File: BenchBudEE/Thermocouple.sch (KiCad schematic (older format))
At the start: 22 parts, among them P2 CONN_3X2, P3 CONN_2, U2 MCP3901, U3 LMT84, U4 OPA4170

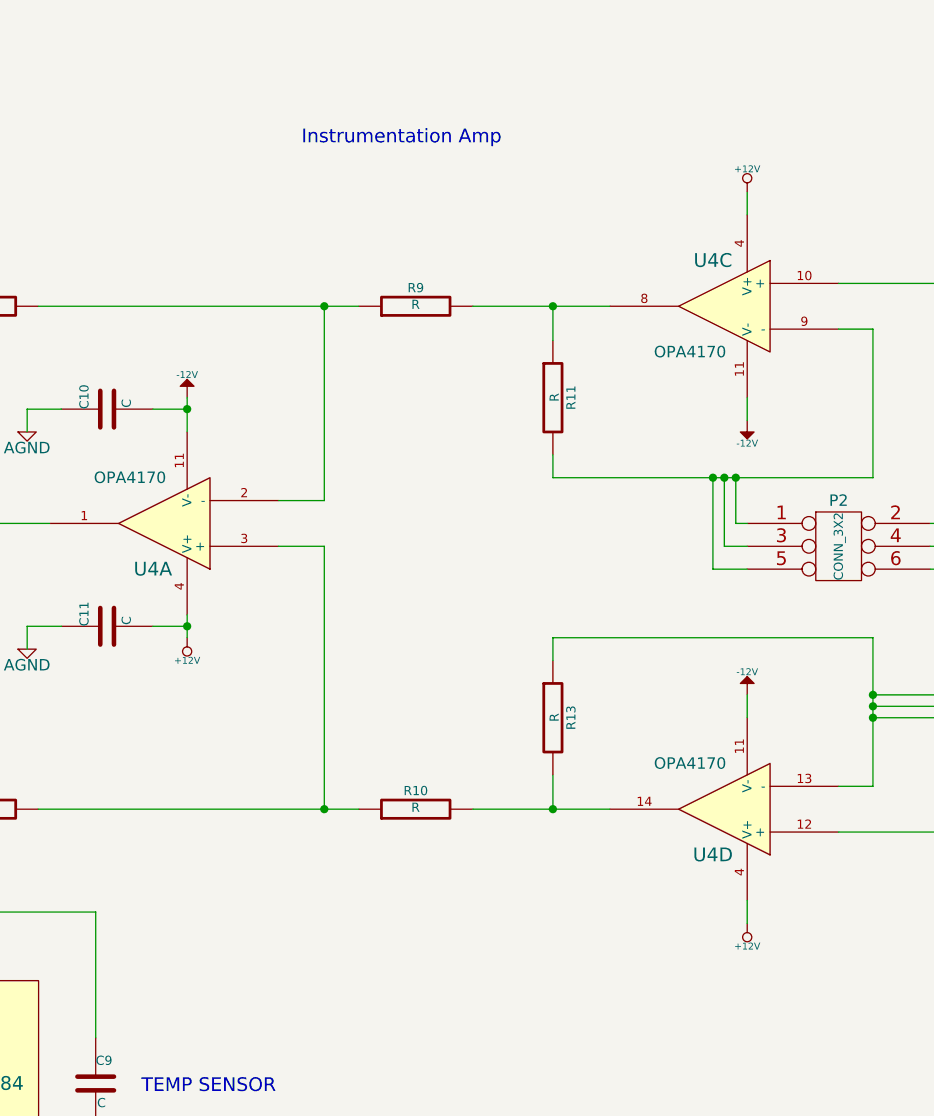
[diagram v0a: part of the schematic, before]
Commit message: Ground and Power Planes
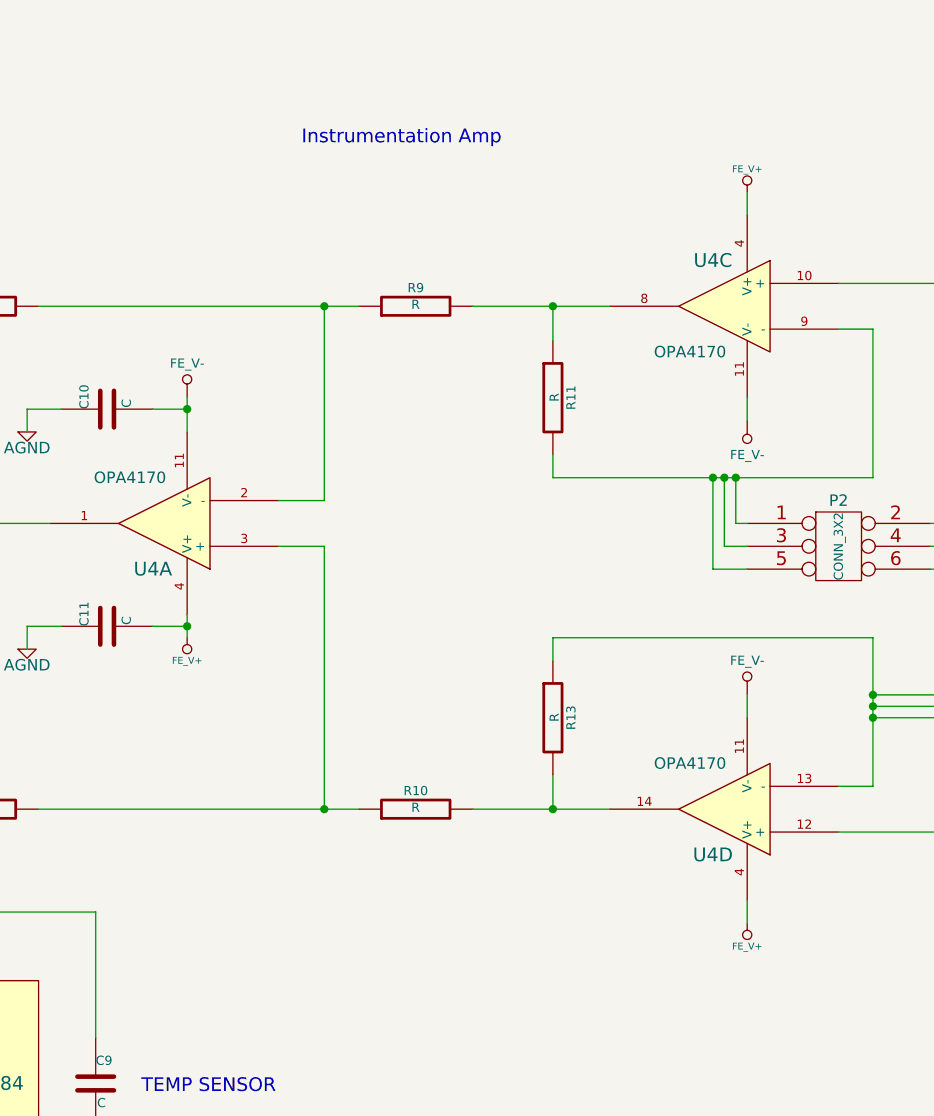
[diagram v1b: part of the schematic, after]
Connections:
- net +12V renamed FE_V+
- net -12V renamed FE_V-
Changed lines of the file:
@@
 Sheet 2 9
 Title ""
-Date "27 feb 2014"
+Date "1 mar 2014"
 Rev ""
 Comp ""
@@
 $EndComp
 $Comp
-L -12V #PWR01
-U 1 1 52F12CF6
-P 6750 2600
-F 0 "#PWR01" H 6750 2730 20  0001 C CNN
-F 1 "-12V" H 6750 2700 30  0000 C CNN
-F 2 "" H 6750 2600 60  0000 C CNN
-F 3 "" H 6750 2600 60  0000 C CNN
-	1    6750 2600
-	1    0    0    -1
-$EndComp
-$Comp
-L -12V #PWR02
-U 1 1 52F12D03
-P 9200 2700
-F 0 "#PWR02" H 9200 2830 20  0001 C CNN
-F 1 "-12V" H 9200 2800 30  0000 C CNN
-F 2 "" H 9200 2700 60  0000 C CNN
-F 3 "" H 9200 2700 60  0000 C CNN
-	1    9200 2700
-	-1   0    0    1
-$EndComp
-$Comp
-L -12V #PWR03
-U 1 1 52F12D09
-P 9200 3900
-F 0 "#PWR03" H 9200 4030 20  0001 C CNN
-F 1 "-12V" H 9200 4000 30  0000 C CNN
-F 2 "" H 9200 3900 60  0000 C CNN
-F 3 "" H 9200 3900 60  0000 C CNN
-	1    9200 3900
-	1    0    0    -1
-$EndComp
-$Comp
-L +12V #PWR04
-U 1 1 52F12D6E
-P 6750 3650
-F 0 "#PWR04" H 6750 3600 20  0001 C CNN
-F 1 "+12V" H 6750 3750 30  0000 C CNN
-F 2 "" H 6750 3650 60  0000 C CNN
-F 3 "" H 6750 3650 60  0000 C CNN
-	1    6750 3650
-	-1   0    0    1
-$EndComp
-$Comp
-L +12V #PWR05
-U 1 1 52F12D7B
-P 9200 1700
-F 0 "#PWR05" H 9200 1650 20  0001 C CNN
-F 1 "+12V" H 9200 1800 30  0000 C CNN
-F 2 "" H 9200 1700 60  0000 C CNN
-F 3 "" H 9200 1700 60  0000 C CNN
-	1    9200 1700
-	1    0    0    -1
-$EndComp
-$Comp
-L +12V #PWR06
-U 1 1 52F12D81
-P 9200 4900
-F 0 "#PWR06" H 9200 4850 20  0001 C CNN
-F 1 "+12V" H 9200 5000 30  0000 C CNN
-F 2 "" H 9200 4900 60  0000 C CNN
-F 3 "" H 9200 4900 60  0000 C CNN
-	1    9200 4900
-	-1   0    0    1
-$EndComp
-$Comp
-L AGND #PWR07
+L AGND #PWR7
 U 1 1 52F12E22
 P 5250 4550
-F 0 "#PWR07" H 5250 4550 40  0001 C CNN
+F 0 "#PWR7" H 5250 4550 40  0001 C CNN
 F 1 "AGND" H 5250 4480 50  0000 C CNN
 F 2 "" H 5250 4550 60  0000 C CNN
@@
 $EndComp
 $Comp
-L AGND #PWR08
+L AGND #PWR8
 U 1 1 52F1304C
 P 5250 6650
-F 0 "#PWR08" H 5250 6650 40  0001 C CNN
+F 0 "#PWR8" H 5250 6650 40  0001 C CNN
 F 1 "AGND" H 5250 6580 50  0000 C CNN
 F 2 "" H 5250 6650 60  0000 C CNN
@@
 $EndComp
 $Comp
-L +5V #PWR09
+L +5V #PWR9
 U 1 1 5303ACCB
 P 5800 4800
-F 0 "#PWR09" H 5800 4890 20  0001 C CNN
+F 0 "#PWR9" H 5800 4890 20  0001 C CNN
 F 1 "+5V" H 5800 4890 30  0000 C CNN
 F 2 "" H 5800 4800 60  0000 C CNN
@@
 $EndComp
 $Comp
-L AGND #PWR010
+L AGND #PWR11
 U 1 1 5303AEFA
 P 6050 3700
-F 0 "#PWR010" H 6050 3700 40  0001 C CNN
+F 0 "#PWR11" H 6050 3700 40  0001 C CNN
 F 1 "AGND" H 6050 3630 50  0000 C CNN
 F 2 "" H 6050 3700 60  0000 C CNN
@@
 $EndComp
 $Comp
-L AGND #PWR011
+L AGND #PWR10
 U 1 1 5303AFBF
 P 6050 2750
-F 0 "#PWR011" H 6050 2750 40  0001 C CNN
+F 0 "#PWR10" H 6050 2750 40  0001 C CNN
 F 1 "AGND" H 6050 2680 50  0000 C CNN
 F 2 "" H 6050 2750 60  0000 C CNN
@@
 $EndComp
 $Comp
-L +5V #PWR012
+L +5V #PWR4
 U 1 1 5303B53D
 P 3200 1550
-F 0 "#PWR012" H 3200 1640 20  0001 C CNN
+F 0 "#PWR4" H 3200 1640 20  0001 C CNN
 F 1 "+5V" H 3200 1640 30  0000 C CNN
 F 2 "" H 3200 1550 60  0000 C CNN
@@
 $EndComp
 $Comp
-L AGND #PWR013
+L AGND #PWR6
 U 1 1 5303B6E8
 P 3850 1800
-F 0 "#PWR013" H 3850 1800 40  0001 C CNN
+F 0 "#PWR6" H 3850 1800 40  0001 C CNN
 F 1 "AGND" H 3850 1730 50  0000 C CNN
 F 2 "" H 3850 1800 60  0000 C CNN
@@
 $EndComp
 $Comp
-L AGND #PWR014
+L AGND #PWR3
 U 1 1 5303B92C
 P 2650 4550
-F 0 "#PWR014" H 2650 4550 40  0001 C CNN
+F 0 "#PWR3" H 2650 4550 40  0001 C CNN
 F 1 "AGND" H 2650 4480 50  0000 C CNN
 F 2 "" H 2650 4550 60  0000 C CNN
@@
 $EndComp
 $Comp
-L AGND #PWR015
+L AGND #PWR5
 U 1 1 5303BA18
 P 3200 4550
-F 0 "#PWR015" H 3200 4550 40  0001 C CNN
+F 0 "#PWR5" H 3200 4550 40  0001 C CNN
 F 1 "AGND" H 3200 4480 50  0000 C CNN
 F 2 "" H 3200 4550 60  0000 C CNN
@@
 $EndComp
 $Comp
-L +5V #PWR016
+L +5V #PWR2
 U 1 1 5303BA92
 P 2650 1550
-F 0 "#PWR016" H 2650 1640 20  0001 C CNN
+F 0 "#PWR2" H 2650 1640 20  0001 C CNN
 F 1 "+5V" H 2650 1640 30  0000 C CNN
 F 2 "" H 2650 1550 60  0000 C CNN
@@
 $EndComp
 $Comp
-L AGND #PWR017
+L AGND #PWR1
 U 1 1 5303BA98
 P 1950 1800
-F 0 "#PWR017" H 1950 1800 40  0001 C CNN
+F 0 "#PWR1" H 1950 1800 40  0001 C CNN
 F 1 "AGND" H 1950 1730 50  0000 C CNN
 F 2 "" H 1950 1800 60  0000 C CNN
@@
 Text HLabel 1050 3000 0    60   Output ~ 0
 MISO
+$Comp
+L FE_V+ #PWR13
+U 1 1 5311A08F
+P 6750 3650
+F 0 "#PWR13" H 6750 3750 30  0001 C CNN
+F 1 "FE_V+" H 6750 3750 30  0000 C CNN
+F 2 "" H 6750 3650 60  0000 C CNN
+F 3 "" H 6750 3650 60  0000 C CNN
+	1    6750 3650
+	-1   0    0    1
+$EndComp
+$Comp
+L FE_V+ #PWR17
+U 1 1 5311A095
+P 9200 4900
+F 0 "#PWR17" H 9200 5000 30  0001 C CNN
+F 1 "FE_V+" H 9200 5000 30  0000 C CNN
+F 2 "" H 9200 4900 60  0000 C CNN
+F 3 "" H 9200 4900 60  0000 C CNN
+	1    9200 4900
+	-1   0    0    1
+$EndComp
+$Comp
+L FE_V+ #PWR14
+U 1 1 5311A09B
+P 9200 1700
+F 0 "#PWR14" H 9200 1800 30  0001 C CNN
+F 1 "FE_V+" H 9200 1800 30  0000 C CNN
+F 2 "" H 9200 1700 60  0000 C CNN
+F 3 "" H 9200 1700 60  0000 C CNN
+	1    9200 1700
+	1    0    0    -1
+$EndComp
+$Comp
+L FE_V- #PWR16
+U 1 1 5311A0A1
+P 9200 3900
+F 0 "#PWR16" H 9200 4100 40  0001 C CNN
+F 1 "FE_V-" H 9200 4050 40  0000 C CNN
+F 2 "~" H 9200 3900 60  0000 C CNN
+F 3 "~" H 9200 3900 60  0000 C CNN
+	1    9200 3900
+	1    0    0    -1
+$EndComp
+$Comp
+L FE_V- #PWR15
+U 1 1 5311A0A7
+P 9200 2700
+F 0 "#PWR15" H 9200 2900 40  0001 C CNN
+F 1 "FE_V-" H 9200 2850 40  0000 C CNN
+F 2 "~" H 9200 2700 60  0000 C CNN
+F 3 "~" H 9200 2700 60  0000 C CNN
+	1    9200 2700
+	-1   0    0    1
+$EndComp
+$Comp
+L FE_V- #PWR12
+U 1 1 5311A0AD
+P 6750 2600
+F 0 "#PWR12" H 6750 2800 40  0001 C CNN
+F 1 "FE_V-" H 6750 2750 40  0000 C CNN
+F 2 "~" H 6750 2600 60  0000 C CNN
+F 3 "~" H 6750 2600 60  0000 C CNN
+	1    6750 2600
+	1    0    0    -1
+$EndComp
 $EndSCHEMATC

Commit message: Layout Work Session 4
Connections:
- net labels added: GND_TC
- net labels removed: AGND
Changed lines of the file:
@@
 Sheet 2 9
 Title ""
-Date "1 mar 2014"
+Date "2 mar 2014"
 Rev ""
 Comp ""
@@
 	0    -1   -1   0
 $EndComp
-$Comp
-L AGND #PWR01
-U 1 1 52F12E22
-P 5250 4550
-F 0 "#PWR01" H 5250 4550 40  0001 C CNN
-F 1 "AGND" H 5250 4480 50  0000 C CNN
-F 2 "" H 5250 4550 60  0000 C CNN
-F 3 "" H 5250 4550 60  0000 C CNN
-	1    5250 4550
-	1    0    0    -1
-$EndComp
-$Comp
-L AGND #PWR02
-U 1 1 52F1304C
-P 5250 6650
-F 0 "#PWR02" H 5250 6650 40  0001 C CNN
-F 1 "AGND" H 5250 6580 50  0000 C CNN
-F 2 "" H 5250 6650 60  0000 C CNN
-F 3 "" H 5250 6650 60  0000 C CNN
-	1    5250 6650
-	1    0    0    -1
-$EndComp
 Text Notes 10100 2500 0    60   ~ 0
 Analog/TC Input
@@
 $EndComp
 $Comp
-L +5V #PWR03
+L +5V #PWR01
 U 1 1 5303ACCB
 P 5800 4800
-F 0 "#PWR03" H 5800 4890 20  0001 C CNN
+F 0 "#PWR01" H 5800 4890 20  0001 C CNN
 F 1 "+5V" H 5800 4890 30  0000 C CNN
 F 2 "" H 5800 4800 60  0000 C CNN
@@
 $EndComp
 $Comp
-L AGND #PWR04
-U 1 1 5303AEFA
-P 6050 3700
-F 0 "#PWR04" H 6050 3700 40  0001 C CNN
-F 1 "AGND" H 6050 3630 50  0000 C CNN
-F 2 "" H 6050 3700 60  0000 C CNN
-F 3 "" H 6050 3700 60  0000 C CNN
-	1    6050 3700
-	1    0    0    -1
-$EndComp
-$Comp
 L C C10
 U 1 1 5303AFB9
@@
 $EndComp
 $Comp
-L AGND #PWR05
-U 1 1 5303AFBF
-P 6050 2750
-F 0 "#PWR05" H 6050 2750 40  0001 C CNN
-F 1 "AGND" H 6050 2680 50  0000 C CNN
-F 2 "" H 6050 2750 60  0000 C CNN
-F 3 "" H 6050 2750 60  0000 C CNN
-	1    6050 2750
-	1    0    0    -1
-$EndComp
-$Comp
-L +5V #PWR06
+L +5V #PWR02
 U 1 1 5303B53D
 P 3200 1550
-F 0 "#PWR06" H 3200 1640 20  0001 C CNN
+F 0 "#PWR02" H 3200 1640 20  0001 C CNN
 F 1 "+5V" H 3200 1640 30  0000 C CNN
 F 2 "" H 3200 1550 60  0000 C CNN
@@
 $EndComp
 $Comp
-L AGND #PWR07
-U 1 1 5303B6E8
-P 3850 1800
-F 0 "#PWR07" H 3850 1800 40  0001 C CNN
-F 1 "AGND" H 3850 1730 50  0000 C CNN
-F 2 "" H 3850 1800 60  0000 C CNN
-F 3 "" H 3850 1800 60  0000 C CNN
-	1    3850 1800
-	1    0    0    -1
-$EndComp
-$Comp
 L C C7
 U 1 1 5303B7CA
@@
 $EndComp
 $Comp
-L AGND #PWR08
-U 1 1 5303B92C
-P 2650 4550
-F 0 "#PWR08" H 2650 4550 40  0001 C CNN
-F 1 "AGND" H 2650 4480 50  0000 C CNN
-F 2 "" H 2650 4550 60  0000 C CNN
-F 3 "" H 2650 4550 60  0000 C CNN
-	1    2650 4550
-	1    0    0    -1
-$EndComp
-$Comp
-L AGND #PWR09
-U 1 1 5303BA18
-P 3200 4550
-F 0 "#PWR09" H 3200 4550 40  0001 C CNN
-F 1 "AGND" H 3200 4480 50  0000 C CNN
-F 2 "" H 3200 4550 60  0000 C CNN
-F 3 "" H 3200 4550 60  0000 C CNN
-	1    3200 4550
-	1    0    0    -1
-$EndComp
-$Comp
-L +5V #PWR010
+L +5V #PWR03
 U 1 1 5303BA92
 P 2650 1550
-F 0 "#PWR010" H 2650 1640 20  0001 C CNN
+F 0 "#PWR03" H 2650 1640 20  0001 C CNN
 F 1 "+5V" H 2650 1640 30  0000 C CNN
 F 2 "" H 2650 1550 60  0000 C CNN
 F 3 "" H 2650 1550 60  0000 C CNN
 	1    2650 1550
-	1    0    0    -1
-$EndComp
-$Comp
-L AGND #PWR011
-U 1 1 5303BA98
-P 1950 1800
-F 0 "#PWR011" H 1950 1800 40  0001 C CNN
-F 1 "AGND" H 1950 1730 50  0000 C CNN
-F 2 "" H 1950 1800 60  0000 C CNN
-F 3 "" H 1950 1800 60  0000 C CNN
-	1    1950 1800
 	1    0    0    -1
 $EndComp
@@
 MISO
 $Comp
-L FE_V+ #PWR012
+L FE_V+ #PWR04
 U 1 1 5311A08F
 P 6750 3650
-F 0 "#PWR012" H 6750 3750 30  0001 C CNN
+F 0 "#PWR04" H 6750 3750 30  0001 C CNN
 F 1 "FE_V+" H 6750 3750 30  0000 C CNN
 F 2 "" H 6750 3650 60  0000 C CNN
@@
 $EndComp
 $Comp
-L FE_V+ #PWR013
+L FE_V+ #PWR05
 U 1 1 5311A095
 P 9200 4900
-F 0 "#PWR013" H 9200 5000 30  0001 C CNN
+F 0 "#PWR05" H 9200 5000 30  0001 C CNN
 F 1 "FE_V+" H 9200 5000 30  0000 C CNN
 F 2 "" H 9200 4900 60  0000 C CNN
@@
 $EndComp
 $Comp
-L FE_V+ #PWR014
+L FE_V+ #PWR06
 U 1 1 5311A09B
 P 9200 1700
-F 0 "#PWR014" H 9200 1800 30  0001 C CNN
+F 0 "#PWR06" H 9200 1800 30  0001 C CNN
 F 1 "FE_V+" H 9200 1800 30  0000 C CNN
 F 2 "" H 9200 1700 60  0000 C CNN
@@
 	1    0    0    -1
 $EndComp
+$Comp
+L GND_TC #PWR07
+U 1 1 5313267D
+P 2650 4550
+F 0 "#PWR07" H 2650 4550 30  0001 C CNN
+F 1 "GND_TC" H 2650 4480 30  0000 C CNN
+F 2 "" H 2650 4550 60  0000 C CNN
+F 3 "" H 2650 4550 60  0000 C CNN
+	1    2650 4550
+	1    0    0    -1
+$EndComp
+$Comp
+L GND_TC #PWR08
+U 1 1 531326BC
+P 3200 4550
+F 0 "#PWR08" H 3200 4550 30  0001 C CNN
+F 1 "GND_TC" H 3200 4480 30  0000 C CNN
+F 2 "" H 3200 4550 60  0000 C CNN
+F 3 "" H 3200 4550 60  0000 C CNN
+	1    3200 4550
+	1    0    0    -1
+$EndComp
+$Comp
+L GND_TC #PWR09
+U 1 1 531326C2
+P 1950 1800
+F 0 "#PWR09" H 1950 1800 30  0001 C CNN
+F 1 "GND_TC" H 1950 1730 30  0000 C CNN
+F 2 "" H 1950 1800 60  0000 C CNN
+F 3 "" H 1950 1800 60  0000 C CNN
+	1    1950 1800
+	1    0    0    -1
+$EndComp
+$Comp
+L GND_TC #PWR010
+U 1 1 531326D2
+P 3850 1800
+F 0 "#PWR010" H 3850 1800 30  0001 C CNN
+F 1 "GND_TC" H 3850 1730 30  0000 C CNN
+F 2 "" H 3850 1800 60  0000 C CNN
+F 3 "" H 3850 1800 60  0000 C CNN
+	1    3850 1800
+	1    0    0    -1
+$EndComp
+$Comp
+L GND_TC #PWR011
+U 1 1 531326D8
+P 6050 2750
+F 0 "#PWR011" H 6050 2750 30  0001 C CNN
+F 1 "GND_TC" H 6050 2680 30  0000 C CNN
+F 2 "" H 6050 2750 60  0000 C CNN
+F 3 "" H 6050 2750 60  0000 C CNN
+	1    6050 2750
+	1    0    0    -1
+$EndComp
+$Comp
+L GND_TC #PWR012
+U 1 1 531326E8
+P 6050 3700
+F 0 "#PWR012" H 6050 3700 30  0001 C CNN
+F 1 "GND_TC" H 6050 3630 30  0000 C CNN
+F 2 "" H 6050 3700 60  0000 C CNN
+F 3 "" H 6050 3700 60  0000 C CNN
+	1    6050 3700
+	1    0    0    -1
+$EndComp
+$Comp
+L GND_TC #PWR013
+U 1 1 531326EE
+P 5250 4550
+F 0 "#PWR013" H 5250 4550 30  0001 C CNN
+F 1 "GND_TC" H 5250 4480 30  0000 C CNN
+F 2 "" H 5250 4550 60  0000 C CNN
+F 3 "" H 5250 4550 60  0000 C CNN
+	1    5250 4550
+	1    0    0    -1
+$EndComp
+$Comp
+L GND_TC #PWR014
+U 1 1 531326FE
+P 5250 6650
+F 0 "#PWR014" H 5250 6650 30  0001 C CNN
+F 1 "GND_TC" H 5250 6580 30  0000 C CNN
+F 2 "" H 5250 6650 60  0000 C CNN
+F 3 "" H 5250 6650 60  0000 C CNN
+	1    5250 6650
+	1    0    0    -1
+$EndComp

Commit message: Layout Work Session 5
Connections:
- net labels added: AGND
- net labels removed: GND_TC
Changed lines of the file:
@@
 $EndComp
 $Comp
-L GND_TC #PWR07
-U 1 1 5313267D
+L AGND #PWR07
+U 1 1 5313730A
 P 2650 4550
-F 0 "#PWR07" H 2650 4550 30  0001 C CNN
-F 1 "GND_TC" H 2650 4480 30  0000 C CNN
+F 0 "#PWR07" H 2650 4550 40  0001 C CNN
+F 1 "AGND" H 2650 4480 50  0000 C CNN
 F 2 "" H 2650 4550 60  0000 C CNN
 F 3 "" H 2650 4550 60  0000 C CNN
@@
 $EndComp
 $Comp
-L GND_TC #PWR08
-U 1 1 531326BC
+L AGND #PWR08
+U 1 1 53137321
 P 3200 4550
-F 0 "#PWR08" H 3200 4550 30  0001 C CNN
-F 1 "GND_TC" H 3200 4480 30  0000 C CNN
+F 0 "#PWR08" H 3200 4550 40  0001 C CNN
+F 1 "AGND" H 3200 4480 50  0000 C CNN
 F 2 "" H 3200 4550 60  0000 C CNN
 F 3 "" H 3200 4550 60  0000 C CNN
@@
 $EndComp
 $Comp
-L GND_TC #PWR09
-U 1 1 531326C2
+L AGND #PWR09
+U 1 1 5313732C
 P 1950 1800
-F 0 "#PWR09" H 1950 1800 30  0001 C CNN
-F 1 "GND_TC" H 1950 1730 30  0000 C CNN
+F 0 "#PWR09" H 1950 1800 40  0001 C CNN
+F 1 "AGND" H 1950 1730 50  0000 C CNN
 F 2 "" H 1950 1800 60  0000 C CNN
 F 3 "" H 1950 1800 60  0000 C CNN
@@
 $EndComp
 $Comp
-L GND_TC #PWR010
-U 1 1 531326D2
+L AGND #PWR010
+U 1 1 5313733C
 P 3850 1800
-F 0 "#PWR010" H 3850 1800 30  0001 C CNN
-F 1 "GND_TC" H 3850 1730 30  0000 C CNN
+F 0 "#PWR010" H 3850 1800 40  0001 C CNN
+F 1 "AGND" H 3850 1730 50  0000 C CNN
 F 2 "" H 3850 1800 60  0000 C CNN
 F 3 "" H 3850 1800 60  0000 C CNN
@@
 $EndComp
 $Comp
-L GND_TC #PWR011
-U 1 1 531326D8
+L AGND #PWR011
+U 1 1 53137342
 P 6050 2750
-F 0 "#PWR011" H 6050 2750 30  0001 C CNN
-F 1 "GND_TC" H 6050 2680 30  0000 C CNN
+F 0 "#PWR011" H 6050 2750 40  0001 C CNN
+F 1 "AGND" H 6050 2680 50  0000 C CNN
 F 2 "" H 6050 2750 60  0000 C CNN
 F 3 "" H 6050 2750 60  0000 C CNN
@@
 $EndComp
 $Comp
-L GND_TC #PWR012
-U 1 1 531326E8
+L AGND #PWR012
+U 1 1 53137352
 P 6050 3700
-F 0 "#PWR012" H 6050 3700 30  0001 C CNN
-F 1 "GND_TC" H 6050 3630 30  0000 C CNN
+F 0 "#PWR012" H 6050 3700 40  0001 C CNN
+F 1 "AGND" H 6050 3630 50  0000 C CNN
 F 2 "" H 6050 3700 60  0000 C CNN
 F 3 "" H 6050 3700 60  0000 C CNN
@@
 $EndComp
 $Comp
-L GND_TC #PWR013
-U 1 1 531326EE
+L AGND #PWR013
+U 1 1 53137362
 P 5250 4550
-F 0 "#PWR013" H 5250 4550 30  0001 C CNN
-F 1 "GND_TC" H 5250 4480 30  0000 C CNN
+F 0 "#PWR013" H 5250 4550 40  0001 C CNN
+F 1 "AGND" H 5250 4480 50  0000 C CNN
 F 2 "" H 5250 4550 60  0000 C CNN
 F 3 "" H 5250 4550 60  0000 C CNN
@@
 $EndComp
 $Comp
-L GND_TC #PWR014
-U 1 1 531326FE
+L AGND #PWR014
+U 1 1 53137372
 P 5250 6650
-F 0 "#PWR014" H 5250 6650 30  0001 C CNN
-F 1 "GND_TC" H 5250 6580 30  0000 C CNN
+F 0 "#PWR014" H 5250 6650 40  0001 C CNN
+F 1 "AGND" H 5250 6580 50  0000 C CNN
 F 2 "" H 5250 6650 60  0000 C CNN
 F 3 "" H 5250 6650 60  0000 C CNN
